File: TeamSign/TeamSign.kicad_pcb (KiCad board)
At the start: 2 copper layers, 240 x 145 mm, 215 parts, among them J1 RJ45, J2 Barrel_Jack_MountingPin, Q1 BSS138, Q2 BSS138, U1 TPS563200, U2 ESP32-Devkit_C_V4

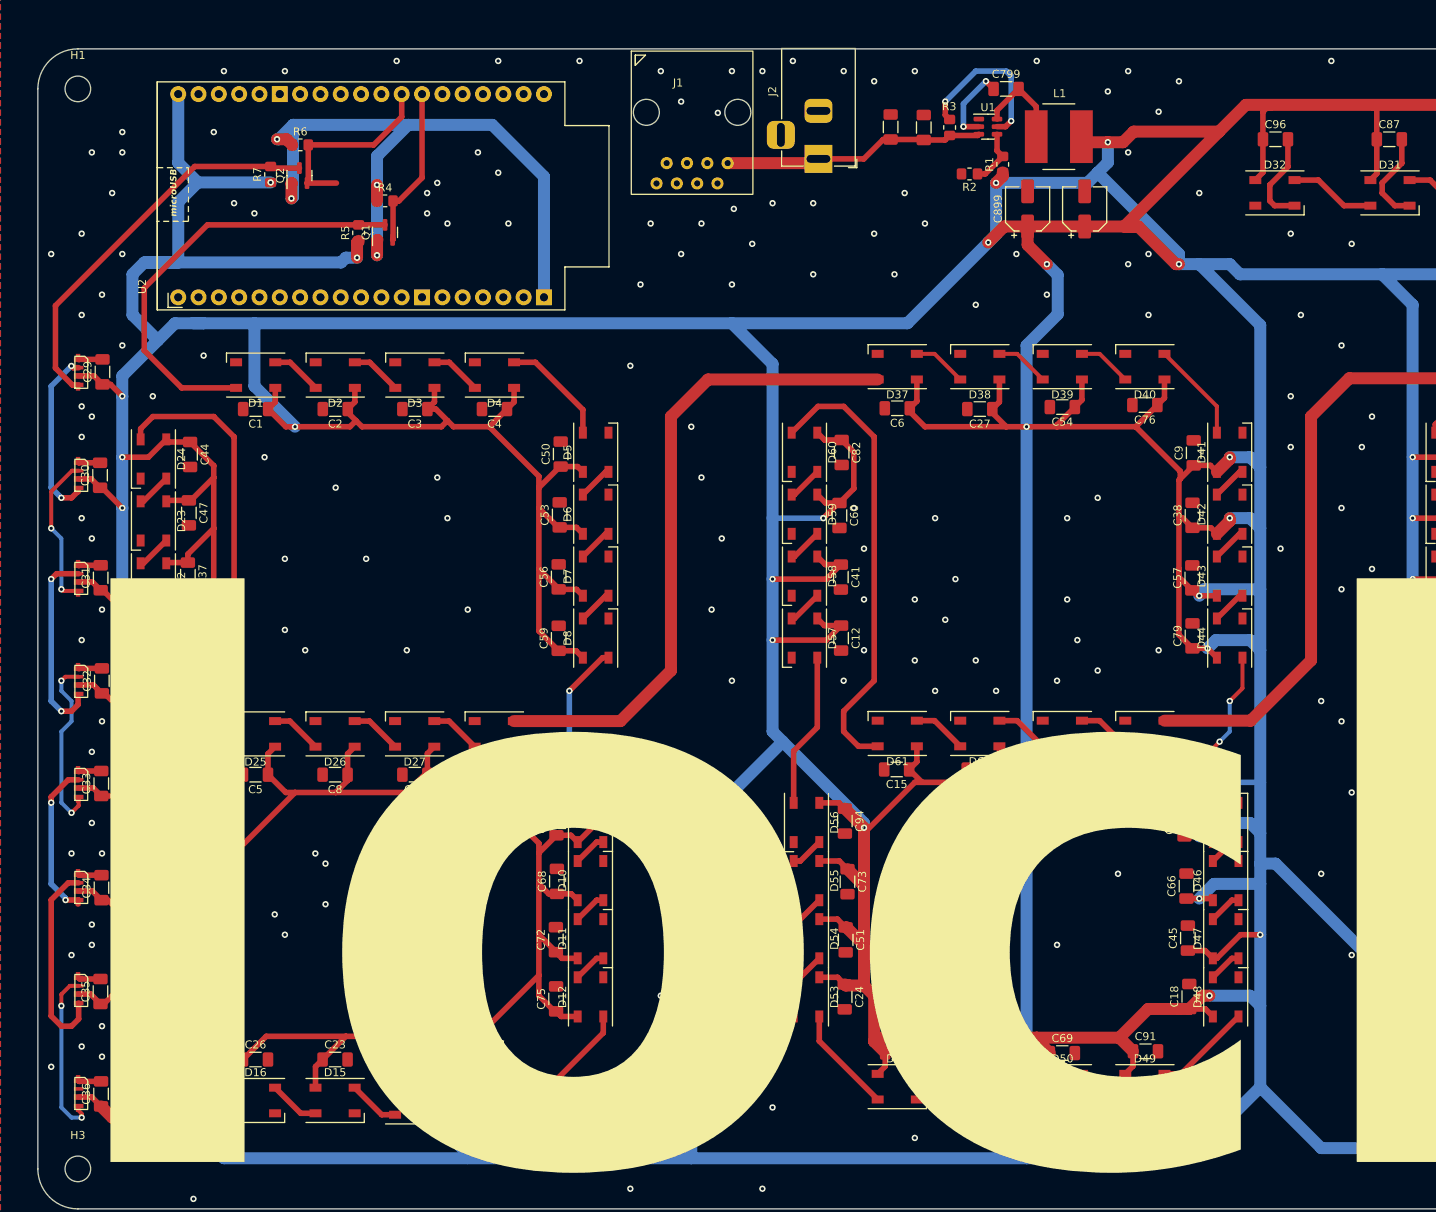
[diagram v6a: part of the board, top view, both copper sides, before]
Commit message: Tiny PCB trace edits.
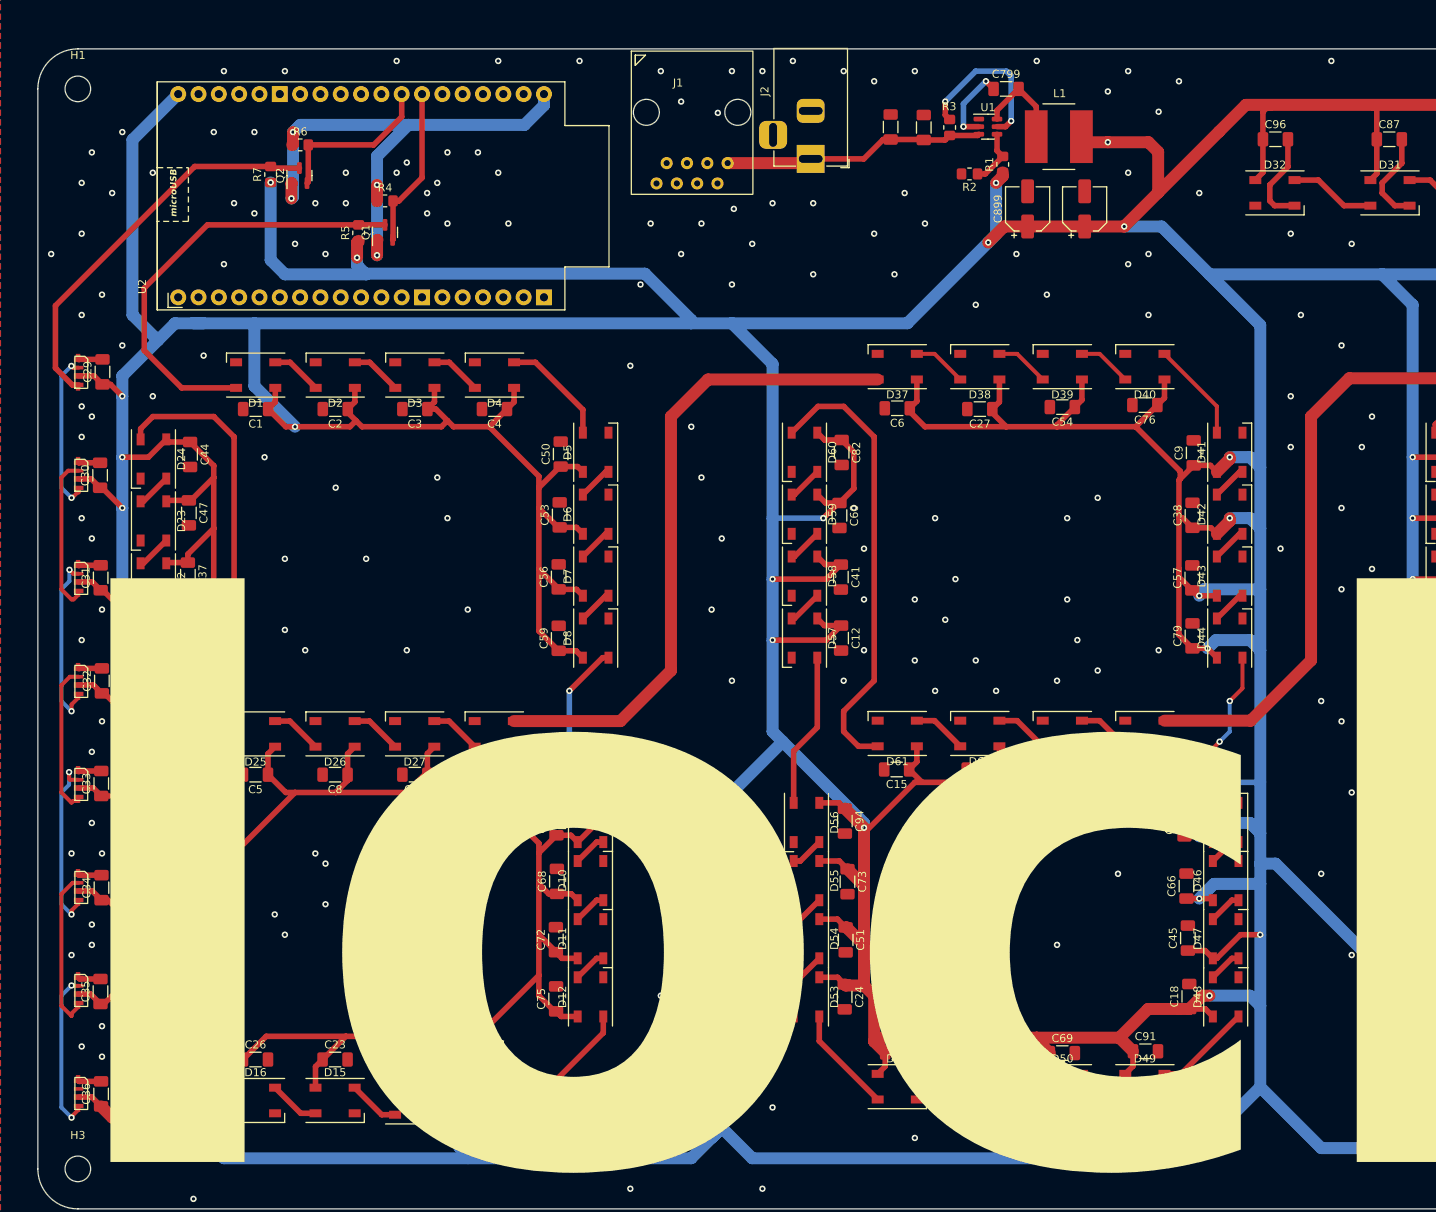
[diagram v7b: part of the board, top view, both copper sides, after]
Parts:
- moved J2 0.97 mm to (121.6, 28.8)
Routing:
- net +5V: track 2745.4 -> 2612.7 mm, vias 48 -> 45
- net +3.3V: track 87.2 -> 68.0 mm
- net Net-(D305-DOUT): track 25.2 -> 20.0 mm
- net Net-(D303-DOUT): track 23.3 -> 19.2 mm, vias 2 -> 0
- net /stacklight_out: track 24.5 -> 20.8 mm
- net Net-(D304-DOUT): track 20.1 -> 22.4 mm
- net Net-(D302-DOUT): track 24.5 -> 22.5 mm
- net Net-(D300-DOUT): track 22.0 -> 20.3 mm
- net Net-(D306-DOUT): track 20.9 -> 19.8 mm
- net Net-(D301-DOUT): track 19.5 -> 19.3 mm, vias 2 -> 0
- net GND: vias 222 -> 230
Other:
- board text added: "be gay do crimes"
